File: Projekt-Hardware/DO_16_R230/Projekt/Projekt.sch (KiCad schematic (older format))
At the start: 39 parts, among them J1 COM_Bus, J2 COM_Bus, K1 DIPxx-1Cxx-51x, K10 DIPxx-1Cxx-51x, K11 DIPxx-1Cxx-51x, K12 DIPxx-1Cxx-51x, K13 DIPxx-1Cxx-51x, K14 DIPxx-1Cxx-51x, K15 DIPxx-1Cxx-51x, K16 DIPxx-1Cxx-51x, K2 DIPxx-1Cxx-51x, K3 DIPxx-1Cxx-51x, K4 DIPxx-1Cxx-51x, K5 DIPxx-1Cxx-51x, K6 DIPxx-1Cxx-51x, K7 DIPxx-1Cxx-51x, K8 DIPxx-1Cxx-51x, K9 DIPxx-1Cxx-51x, SW1 Accept Adress, U1 ATmega328P-PU, X1 DO 16-2

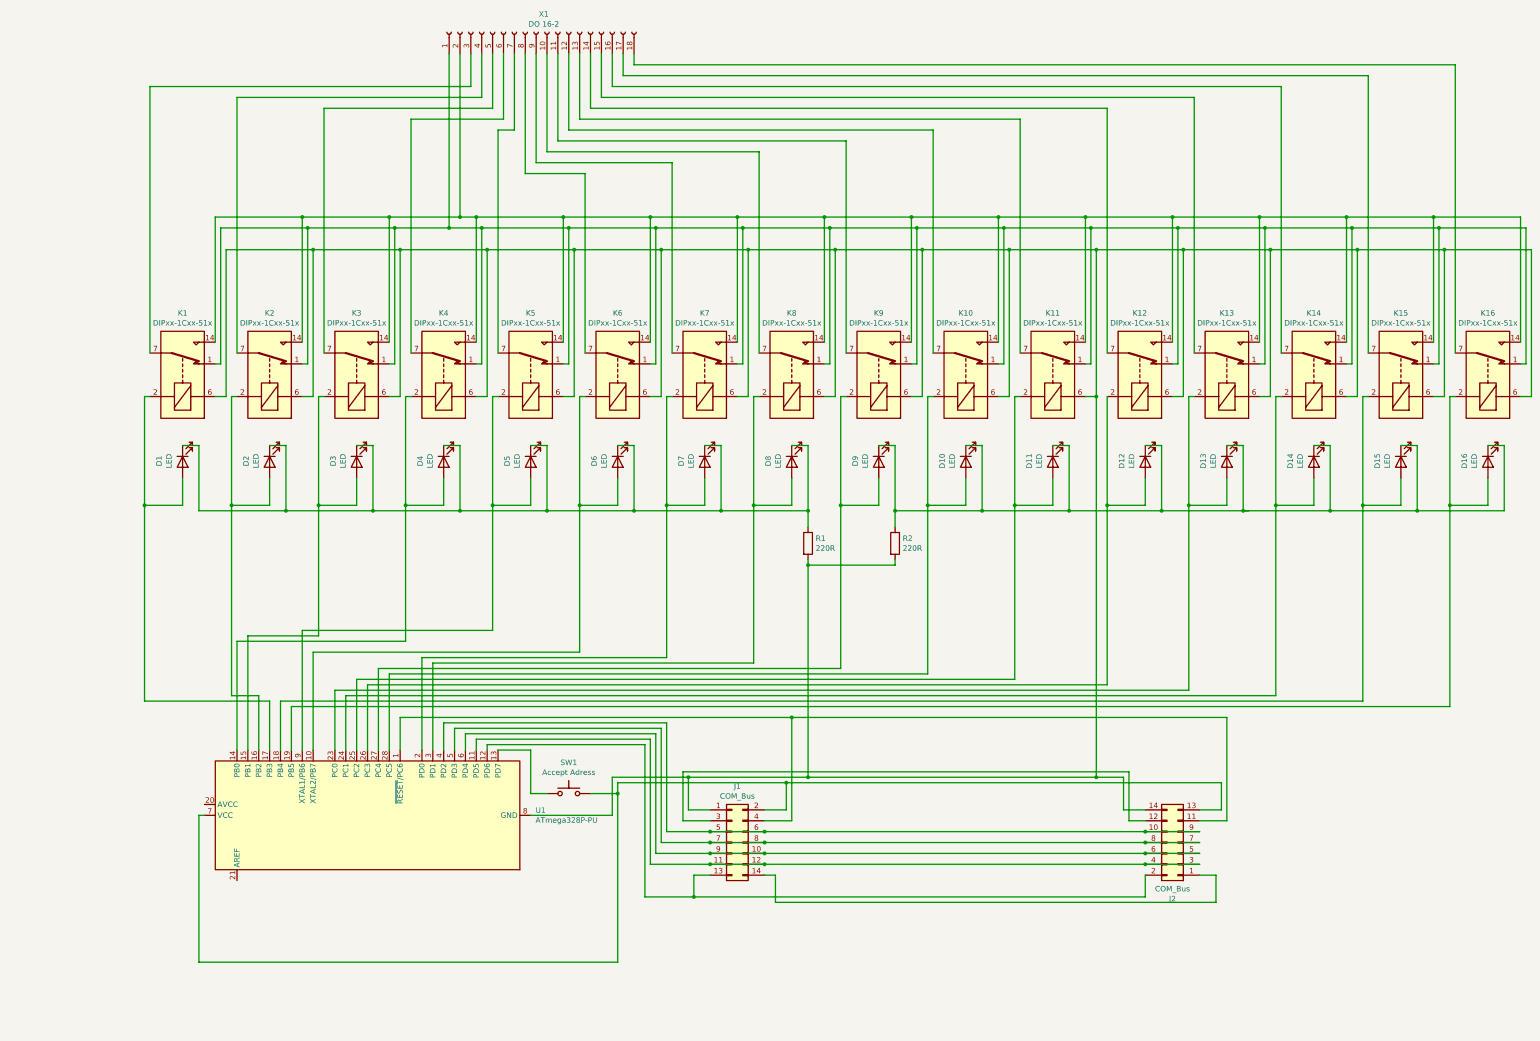
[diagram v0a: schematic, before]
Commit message: Erster (meschanischer) Entwurf für DO_16_R230 Modul
Erster Entwurf für meschanische Bauteile des
DO_16_R230 Moduls:
- Entwurf für Leiterplatten
Fehlende Entwürfe:
- Gehäuse
- Halterungen
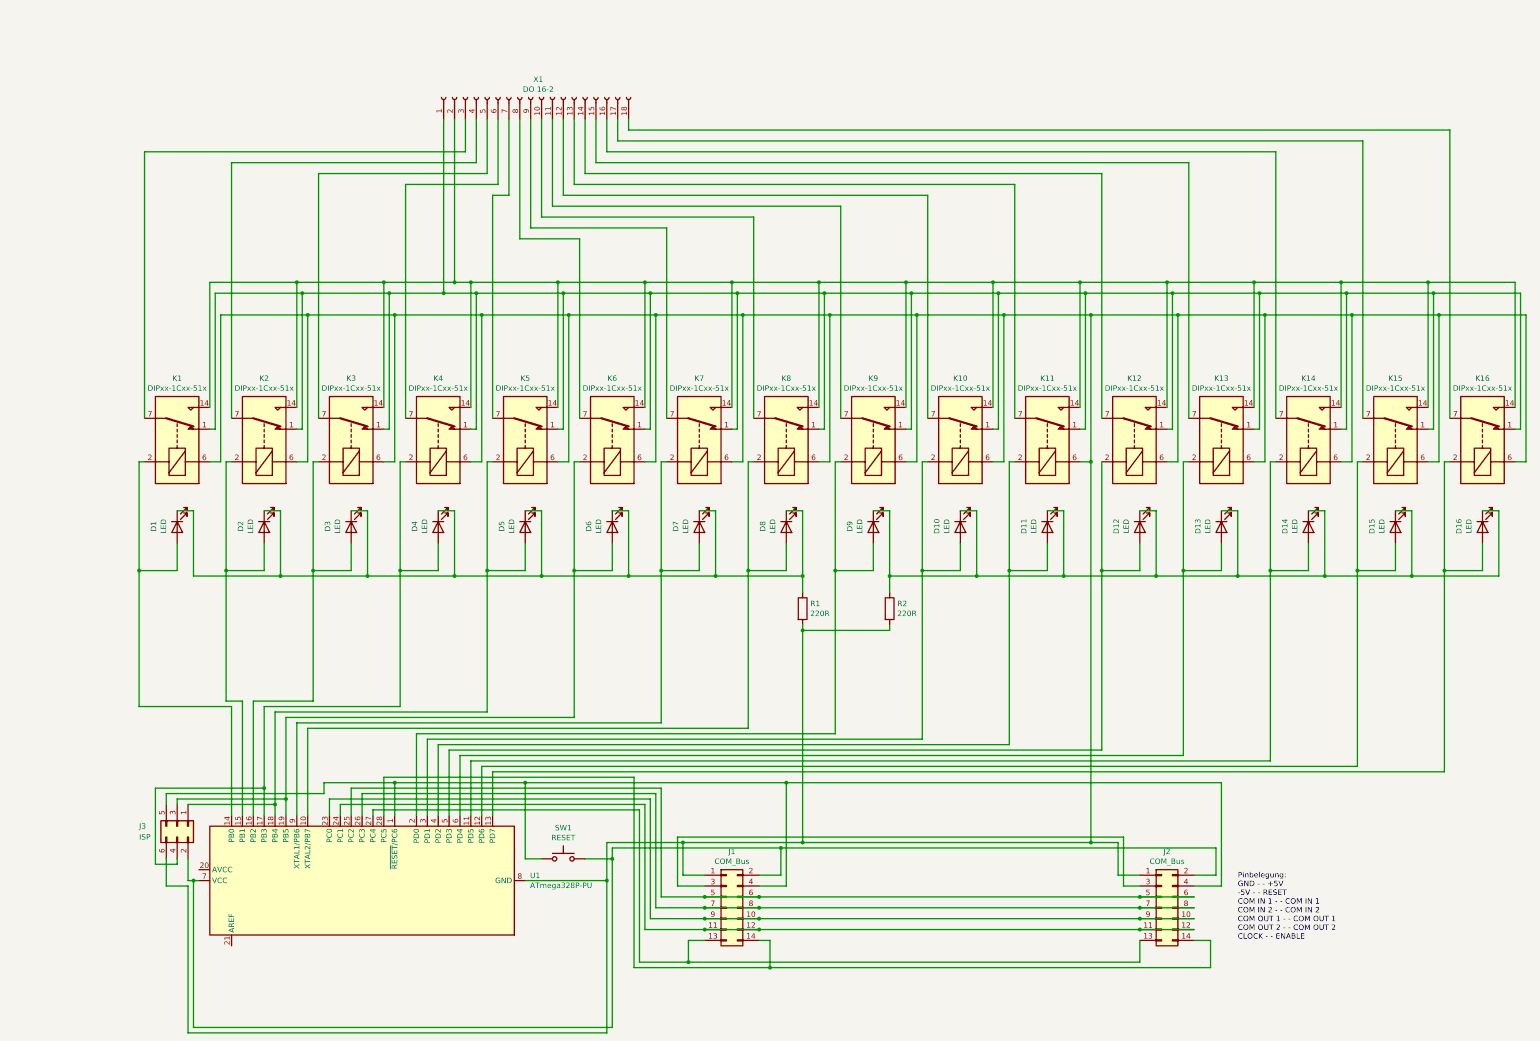
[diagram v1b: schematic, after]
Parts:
- added J3: ISP, Footprints:IDC-Header_2x03_P2.54mm_Vertical, symbol Connector_Generic:Conn_02x03_Odd_Even
- SW1: value Accept Adress -> RESET; footprint (none) -> Button_Switch_THT:SW_PUSH_6mm_H8mm
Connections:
- net at D7.2 (A), K7.2: now also U1.9 (XTAL1/PB6); no longer U1.2 (PD0)
- net at J1.1 (Pin_1), K1.6, K10.6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: now also J2.1 (Pin_1), J3.6 (Pin_6); no longer J2.14 (Pin_14)
- net at D6.2 (A), K6.2: now also U1.19 (PB5), J3.3 (Pin_3); no longer U1.10 (XTAL2/PB7)
- net at D9.2 (A), K9.2: now also U1.2 (PD0); no longer U1.27 (PC4)
- net at D8.2 (A), K8.2: now also U1.10 (XTAL2/PB7); no longer U1.3 (PD1)
- net at D5.2 (A), K5.2: now also U1.18 (PB4), J3.1 (Pin_1); no longer U1.9 (XTAL1/PB6)
- net at D4.2 (A), K4.2: now also U1.17 (PB3), J3.4 (Pin_4); no longer U1.14 (PB0)
- net at D10.2 (A), K10.2: now also U1.3 (PD1); no longer U1.28 (PC5)
- net at D11.2 (A), K11.2: now also U1.4 (PD2); no longer U1.25 (PC2)
- net at D3.2 (A), K3.2: now also U1.16 (PB2); no longer U1.15 (PB1)
- net at D2.2 (A), K2.2: now also U1.15 (PB1); no longer U1.16 (PB2)
- net at D1.2 (A), K1.2: now also U1.14 (PB0); no longer U1.17 (PB3)
- net at J1.4 (Pin_4), U1.1 (~RESET~/PC6): now also J2.4 (Pin_4), SW1.1, J3.5 (Pin_5); no longer J2.11 (Pin_11)
- net at U1.13 (PD7): now also D16.2 (A), K16.2; no longer SW1.1
- net at D15.2 (A), K15.2: now also U1.12 (PD6); no longer U1.18 (PB4)
- net at D13.2 (A), K13.2: now also U1.6 (PD4); no longer U1.23 (PC0)
- net at D14.2 (A), K14.2: now also U1.11 (PD5); no longer U1.24 (PC1)
- net at D12.2 (A), K12.2: now also U1.5 (PD3); no longer U1.26 (PC3)
- net at J1.7 (Pin_7), J1.8 (Pin_8), J2.7 (Pin_7)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: now also U1.26 (PC3); no longer U1.5 (PD3)
- net at J1.2 (Pin_2), SW1.2, U1.7 (VCC): now also J2.2 (Pin_2), J3.2 (Pin_2); no longer J2.13 (Pin_13)
- net at J1.14 (Pin_14): now also J2.14 (Pin_14), U1.28 (PC5); no longer J2.1 (Pin_1)
- net at J2.12 (Pin_12): now also J1.11 (Pin_11), J1.12 (Pin_12), J2.11 (Pin_11), U1.24 (PC1); no longer J1.3 (Pin_3)
- new net: J1.10 (Pin_10), J1.9 (Pin_9), J2.10 (Pin_10), J2.9 (Pin_9), U1.23 (PC0)
- new net: J1.5 (Pin_5), J1.6 (Pin_6), J2.5 (Pin_5), J2.6 (Pin_6), U1.25 (PC2)
- new net: J1.13 (Pin_13), J2.13 (Pin_13), U1.27 (PC4)
- new net: J1.3 (Pin_3), J2.3 (Pin_3)
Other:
- note added: "Pinbelegung:\nGND - - +5V\n-5V - - RESET\nCOM IN 1 - - COM IN 1\nCOM IN 2 - - COM IN 2\nCOM OUT 1 - - COM OUT 1\nCOM OUT 2 - - COM OUT 2\nCLOCK - - ENABLE"
- moved on the sheet: D1, D10, D11, D12, D13, D14, D15, D16, D2, D3, D4, D5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

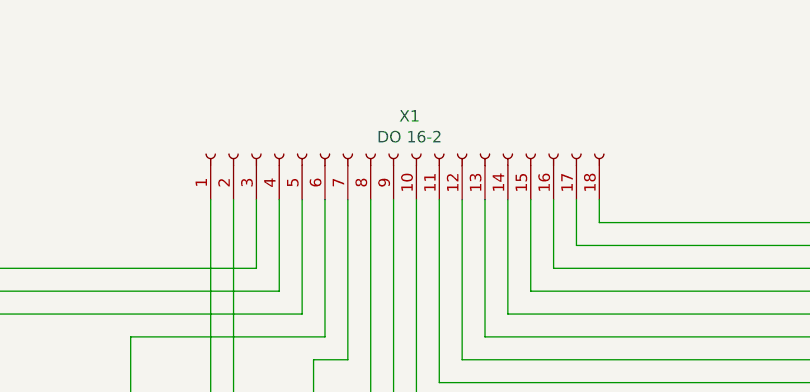
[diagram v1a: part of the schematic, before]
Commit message: Gehäuse für DO_16_R230 begonnen
Angefangen Gehäuse für DO_16_R230
angefangen zu entwerfen.
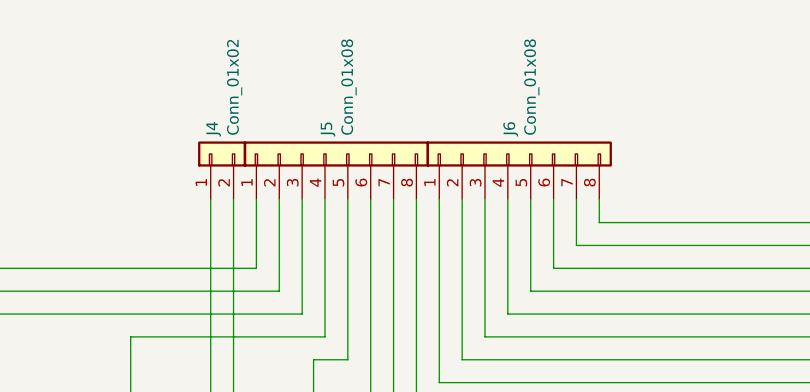
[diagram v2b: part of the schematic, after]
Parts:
- removed X1: DO 16-2, Footprints:Klemmleiste_R5mm_B8mm_Kopie, symbol Connector:Conn_01x18_Female
- added J4: Conn_01x02, Footprints:RND_Steckklemme_2, symbol Connector_Generic:Conn_01x02
- added J5, J6: Conn_01x08, Footprints:RND_Steckklemme_8, symbol Connector_Generic:Conn_01x08
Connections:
- net at K1.1, K10.1, K11.1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: now also J4.1 (Pin_1)
- net at K1.14, K10.14, K11.14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: now also J4.2 (Pin_2)
- net at K7.7, K7.8: now also J5.7 (Pin_7)
- net at K6.7, K6.8: now also J5.6 (Pin_6)
- net at K9.7, K9.8: now also J6.1 (Pin_1)
- net at K8.7, K8.8: now also J5.8 (Pin_8)
- net at K5.7, K5.8: now also J5.5 (Pin_5)
- net at K4.7, K4.8: now also J5.4 (Pin_4)
- net at K10.7, K10.8: now also J6.2 (Pin_2)
- net at K11.7, K11.8: now also J6.3 (Pin_3)
- net at K3.7, K3.8: now also J5.3 (Pin_3)
- net at K2.7, K2.8: now also J5.2 (Pin_2)
- net at K1.7, K1.8: now also J5.1 (Pin_1)
- net at K12.7, K12.8: now also J6.4 (Pin_4)
- net at K13.7, K13.8: now also J6.5 (Pin_5)
- net at K14.7, K14.8: now also J6.6 (Pin_6)
- net at K15.7, K15.8: now also J6.7 (Pin_7)
- net at K16.7, K16.8: now also J6.8 (Pin_8)
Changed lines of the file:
@@
 Wire Wire Line
 	4550 3100 5050 3100
-$Comp
-L Connector:Conn_01x18_Female X1
-U 1 1 60D510A4
-P 5850 1300
-F 0 "X1" V 6015 1230 50  0000 C CNN
-F 1 "DO 16-2" V 5924 1230 50  0000 C CNN
-F 2 "Footprints:Klemmleiste_R5mm_B8mm_Kopie" H 5850 1300 50  0001 C CNN
-F 3 "~" H 5850 1300 50  0001 C CNN
-	1    5850 1300
-	0    -1   -1   0
-$EndComp
 Wire Wire Line
 	12100 9050 11950 9050
@@
 Wire Wire Line
 	12350 5700 13150 5700
+$Comp
+L Connector_Generic:Conn_01x08 J6
+U 1 1 5FE4606B
+P 6350 1300
+F 0 "J6" H 6430 1292 50  0000 L CNN
+F 1 "Conn_01x08" H 6430 1201 50  0000 L CNN
+F 2 "Footprints:RND_Steckklemme_8" H 6350 1300 50  0001 C CNN
+F 3 "~" H 6350 1300 50  0001 C CNN
+	1    6350 1300
+	0    -1   -1   0
+$EndComp
+$Comp
+L Connector_Generic:Conn_01x08 J5
+U 1 1 5FE8513C
+P 5550 1300
+F 0 "J5" H 5630 1292 50  0000 L CNN
+F 1 "Conn_01x08" H 5630 1201 50  0000 L CNN
+F 2 "Footprints:RND_Steckklemme_8" H 5550 1300 50  0001 C CNN
+F 3 "~" H 5550 1300 50  0001 C CNN
+	1    5550 1300
+	0    -1   -1   0
+$EndComp
+$Comp
+L Connector_Generic:Conn_01x02 J4
+U 1 1 5FEC149D
+P 5050 1300
+F 0 "J4" H 5130 1292 50  0000 L CNN
+F 1 "Conn_01x02" H 5130 1201 50  0000 L CNN
+F 2 "Footprints:RND_Steckklemme_2" H 5050 1300 50  0001 C CNN
+F 3 "~" H 5050 1300 50  0001 C CNN
+	1    5050 1300
+	0    -1   -1   0
+$EndComp
 $EndSCHEMATC

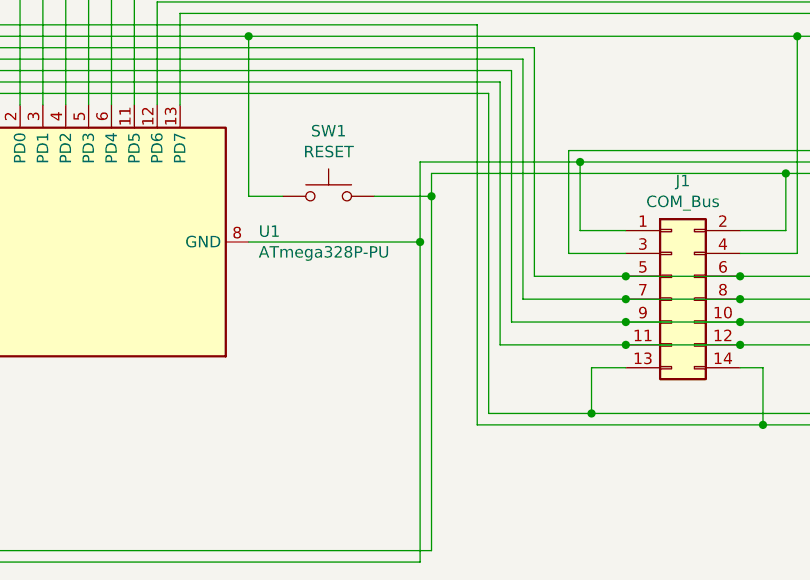
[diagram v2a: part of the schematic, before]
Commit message: Korrektur im Schaltplan
RESET Taster auf von +5V auf GND verschoben.
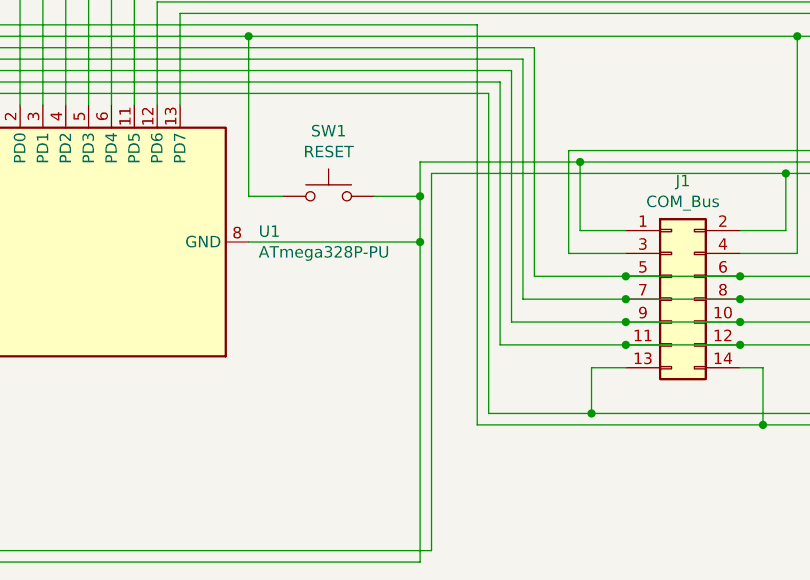
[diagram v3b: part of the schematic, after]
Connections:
- net at J1.1 (Pin_1), J2.1 (Pin_1), J3.6 (Pin_6)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: now also SW1.2
- net at J1.2 (Pin_2), J2.2 (Pin_2), J3.2 (Pin_2)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: no longer SW1.2
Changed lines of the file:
@@
 Wire Wire Line
 	5950 8300 5800 8300
-Wire Wire Line
-	6600 8300 6600 8200
-Wire Wire Line
-	6350 8300 6600 8300
 $Comp
 L Switch:SW_Push SW1
@@
 Wire Wire Line
 	12100 9050 11950 9050
-Connection ~ 6600 8300
-Wire Wire Line
-	6600 9850 6600 8300
 Wire Wire Line
 	2750 9850 6600 9850
@@
 	2800 8500 2750 8500
 Wire Wire Line
-	6550 8500 6550 8150
+	6550 8500 6550 8300
 Wire Wire Line
 	5800 8500 6550 8500
@@
 	0    -1   -1   0
 $EndComp
+Wire Wire Line
+	6600 8200 6600 9850
+Wire Wire Line
+	6350 8300 6550 8300
+Connection ~ 6550 8300
+Wire Wire Line
+	6550 8300 6550 8150
 $EndSCHEMATC

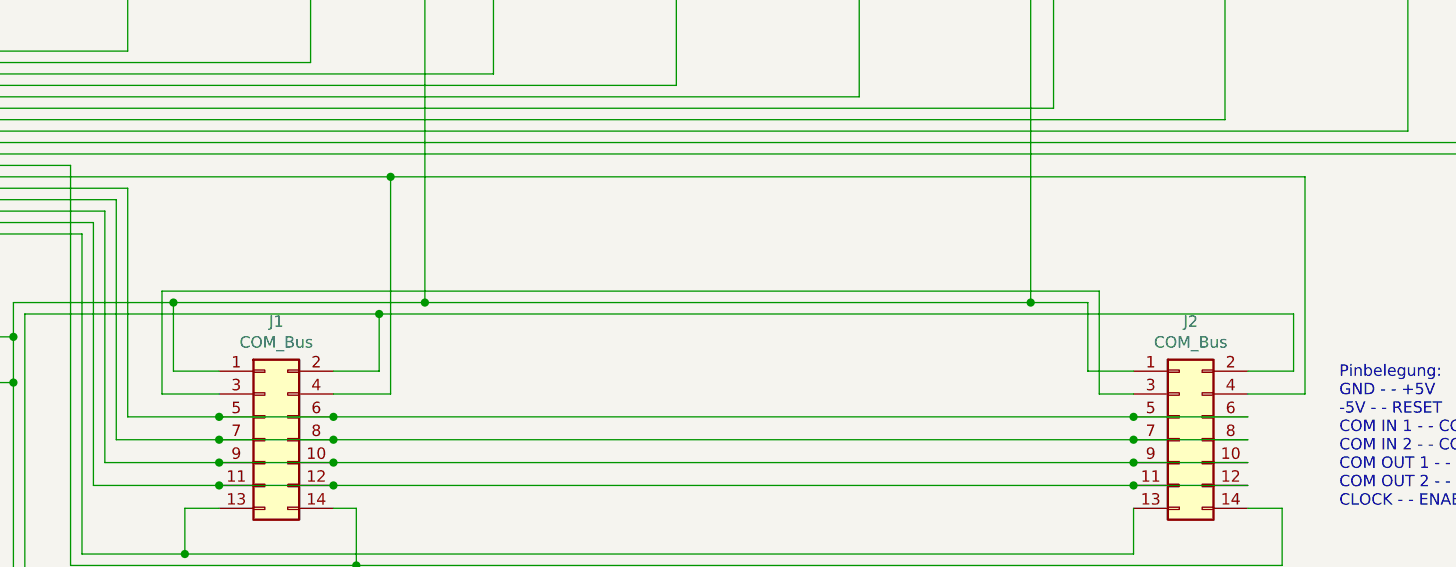
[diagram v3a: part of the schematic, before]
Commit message: Anpassungen Gehäuse + CNC Experimente
Anpassungen des Gehäuses an die Leiteplatte

Angefangen mit Tests für das herstellen der Leiterplatte mit einer CNC Fräse
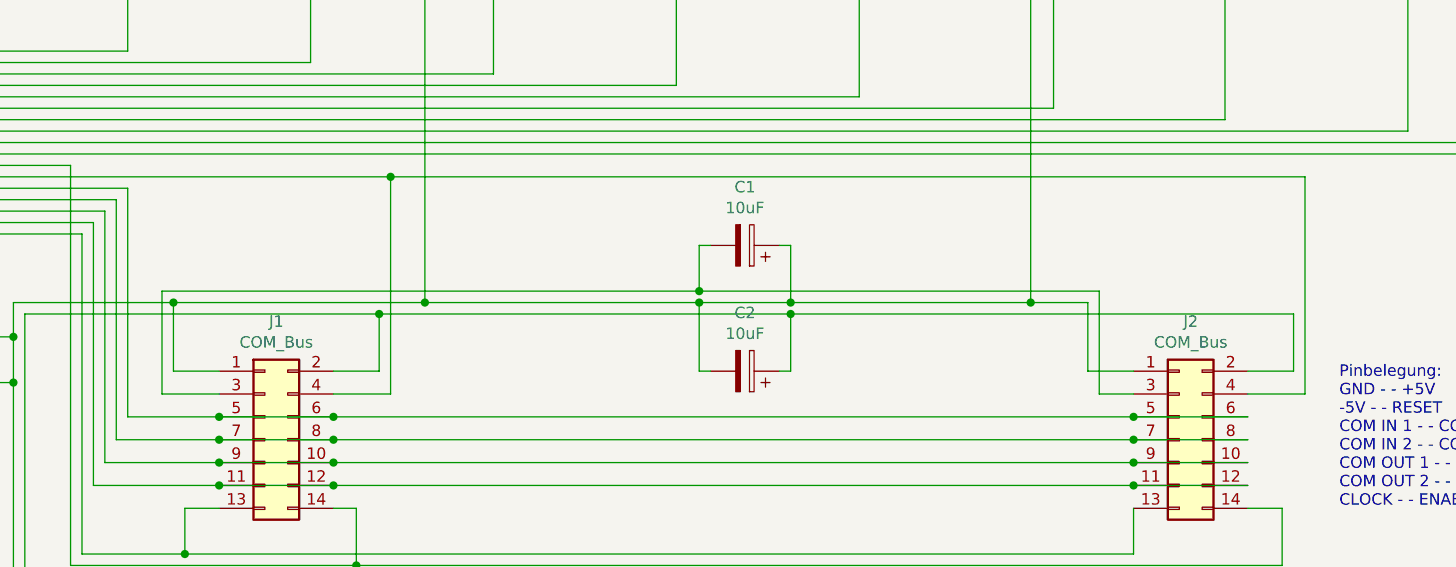
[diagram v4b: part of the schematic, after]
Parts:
- added C1, C2: 10uF, Capacitor_THT:CP_Radial_D6.3mm_P2.50mm, symbol Device:CP
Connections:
- net at J1.1 (Pin_1), J2.1 (Pin_1), J3.6 (Pin_6)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: now also C1.1, C2.2
- net at J1.2 (Pin_2), J2.2 (Pin_2), J3.2 (Pin_2)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: now also C2.1
- net at J1.3 (Pin_3), J2.3 (Pin_3): now also C1.2
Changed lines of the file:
@@
 Wire Wire Line
 	7450 8650 7950 8650
-Connection ~ 7950 8650
 Connection ~ 7450 8750
 Wire Wire Line
@@
 	11950 8450 12150 8450
 Wire Wire Line
-	7200 8100 11300 8100
-Wire Wire Line
 	11300 8550 11300 8100
 Wire Wire Line
@@
 	9950 5100 9950 5700
 Wire Wire Line
-	8350 8150 11000 8150
+	8350 8150 9550 8150
 Connection ~ 8350 8150
 Wire Wire Line
@@
 Wire Wire Line
 	11950 8650 11450 8650
-Wire Wire Line
-	7950 8650 11450 8650
 Wire Wire Line
 	11450 8850 11950 8850
@@
 	8150 8450 7950 8450
 Wire Wire Line
-	8150 8200 12150 8200
-Wire Wire Line
 	6600 8200 8150 8200
 Connection ~ 8150 8200
@@
 Wire Wire Line
 	7950 8950 11450 8950
-Connection ~ 11450 8650
 Connection ~ 11450 8750
 Connection ~ 11450 8850
@@
 Wire Wire Line
 	6550 8300 6550 8150
+Wire Wire Line
+	8150 8200 9950 8200
+Wire Wire Line
+	7200 8100 9550 8100
+Connection ~ 11450 8650
+Connection ~ 7950 8650
+Wire Wire Line
+	7950 8650 11450 8650
+$Comp
+L Device:CP C1
+U 1 1 60095F7F
+P 9750 7900
+F 0 "C1" V 10005 7900 50  0000 C CNN
+F 1 "10uF" V 9914 7900 50  0000 C CNN
+F 2 "Capacitor_THT:CP_Radial_D6.3mm_P2.50mm" H 9788 7750 50  0001 C CNN
+F 3 "~" H 9750 7900 50  0001 C CNN
+	1    9750 7900
+	0    1    -1   0
+$EndComp
+$Comp
+L Device:CP C2
+U 1 1 600D41B0
+P 9750 8450
+F 0 "C2" V 10005 8450 50  0000 C CNN
+F 1 "10uF" V 9914 8450 50  0000 C CNN
+F 2 "Capacitor_THT:CP_Radial_D6.3mm_P2.50mm" H 9788 8300 50  0001 C CNN
+F 3 "~" H 9750 8450 50  0001 C CNN
+	1    9750 8450
+	0    1    -1   0
+$EndComp
+Wire Wire Line
+	9900 8450 9950 8450
+Wire Wire Line
+	9950 8450 9950 8200
+Connection ~ 9950 8200
+Wire Wire Line
+	9950 8200 12150 8200
+Wire Wire Line
+	9600 8450 9550 8450
+Wire Wire Line
+	9550 8450 9550 8150
+Connection ~ 9550 8150
+Wire Wire Line
+	9550 8150 9950 8150
+Wire Wire Line
+	9900 7900 9950 7900
+Wire Wire Line
+	9950 7900 9950 8150
+Connection ~ 9950 8150
+Wire Wire Line
+	9950 8150 11000 8150
+Wire Wire Line
+	9550 7900 9550 8100
+Connection ~ 9550 8100
+Wire Wire Line
+	9550 8100 11300 8100
+Wire Wire Line
+	9550 7900 9600 7900
 $EndSCHEMATC
